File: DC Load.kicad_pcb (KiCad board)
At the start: 2 copper layers, 111 parts, among them IC1 REF7050QDGKR, IC10 REF7050QDGKR, IC11 ISO7740FQDBQRQ1, IC12 ISO7741FQDBQRQ1, IC13 INA826AID, IC14 OPA210IDGKR, IC15 INA296A3IDDFR, IC2 MAX5719GSD+, IC3 REF7050QDGKR, IC4 AD7175-2BRUZ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

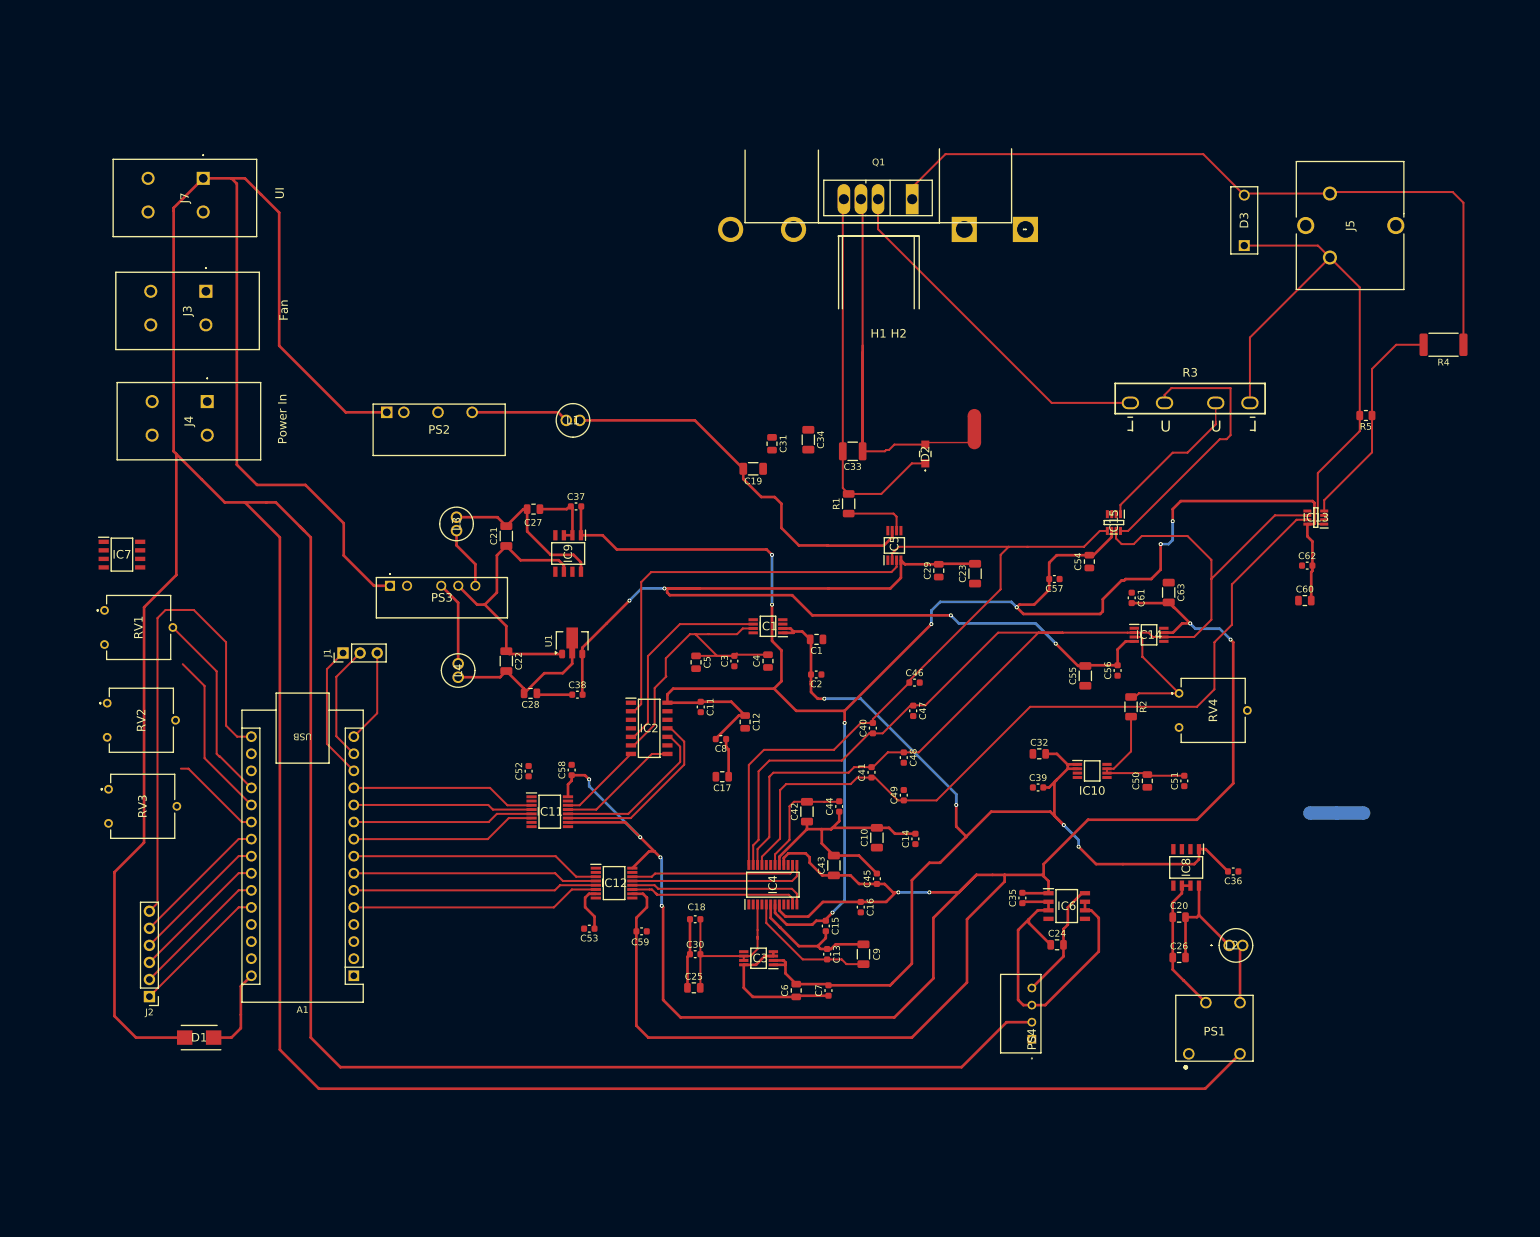
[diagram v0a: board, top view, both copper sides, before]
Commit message: Finished laying out all the traces and adding the temperature sensing circuitry
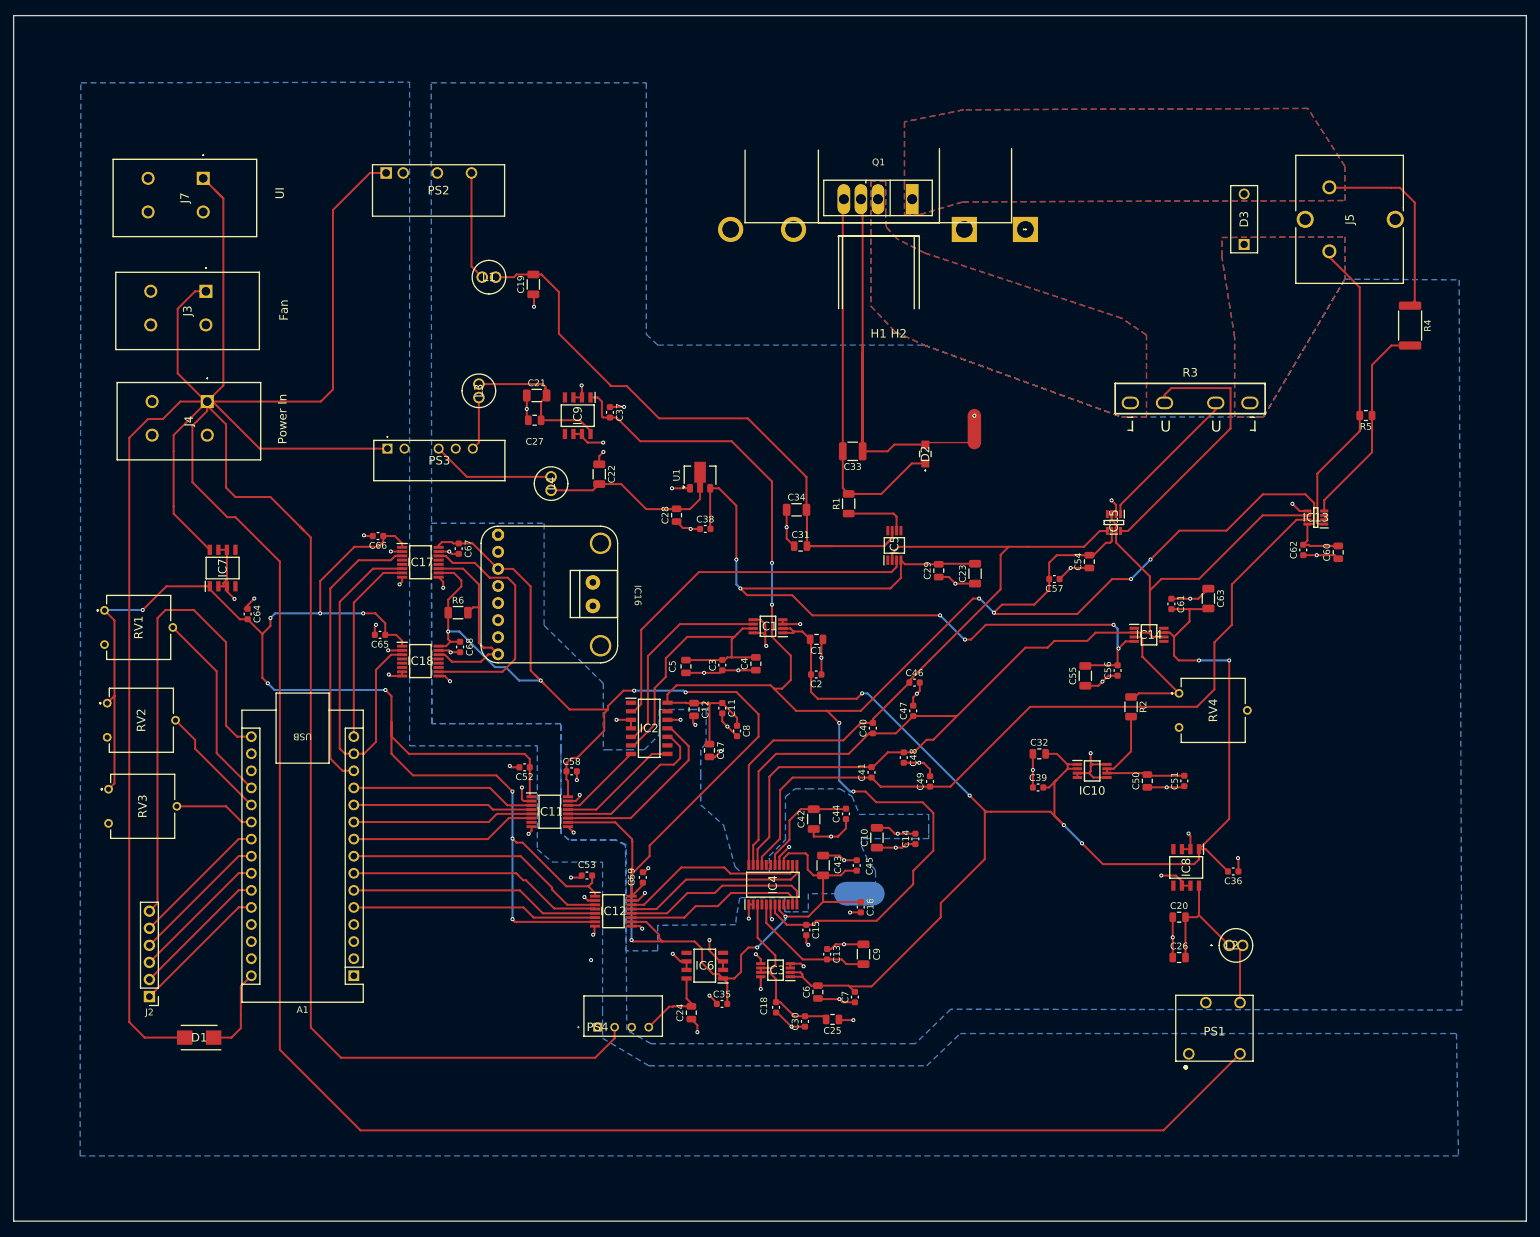
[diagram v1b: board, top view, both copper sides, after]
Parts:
- removed J1: Conn_01x03, Connector_PinHeader_2.54mm:PinHeader_1x03_P2.54mm_Vertical
- removed NT1: Isolated Ground Tie, NetTie:NetTie-3_SMD_Pad2.0mm
- added C64: 0.1u, Capacitor_SMD:C_0603_1608Metric, F.Cu at (69.8, 114.0)
- added C65: 0.1u, Capacitor_SMD:C_0603_1608Metric, F.Cu at (89.5, 117.1)
- added C66: 0.1u, Capacitor_SMD:C_0603_1608Metric, F.Cu at (89.2, 102.4)
- added C67: 0.1u, Capacitor_SMD:C_0603_1608Metric, F.Cu at (101.2, 104.3)
- added C68: 0.1u, Capacitor_SMD:C_0603_1608Metric, F.Cu at (101.4, 118.9)
- added IC16: MAX31850K, Adafruit:MAX31850K, F.Cu at (117.1, 111.2)
- added IC17: ISO7741FQDBQRQ1, ISO7741FQDBQRQ1:SOP64P600X175-16N, F.Cu at (95.5, 106.3)
- added IC18: ISO7741FQDBQRQ1, ISO7741FQDBQRQ1:SOP64P600X175-16N, F.Cu at (95.5, 121.0)
- added NT3: NetTie_2, NetTie:NetTie-2_SMD_Pad2.0mm, B.Cu at (160.8, 155.6)
- added R6: 4.7k, Resistor_SMD:R_1206_3216Metric, F.Cu at (101.1, 113.8)
- moved PS4 64.6 mm to (121.8, 175.4), turned to 0 degrees
- moved C24 55.3 mm to (135.8, 173.3), turned to 90 degrees
- moved IC6 54.6 mm to (137.8, 166.3), turned to 180 degrees
- moved C35 47.4 mm to (140.4, 172.0), turned to 0 degrees
- moved C19 42.7 mm to (112.3, 65.0), turned to 90 degrees
- moved PS2 35.6 mm to (90.4, 48.4)
- moved C28 34.3 mm to (133.6, 99.3), turned to 90 degrees
- moved C38 31.1 mm to (137.9, 101.3)
- moved U1 31.1 mm to (137.1, 93.3)
- moved L4 31.0 mm to (114.9, 95.6)
- moved C22 31.0 mm to (122.1, 93.2)
- moved L1 24.7 mm to (106.7, 63.9)
- moved C21 21.4 mm to (112.8, 81.5), turned to 0 degrees
- moved C25 21.2 mm to (156.8, 174.3), turned to 180 degrees
- moved IC9 20.5 mm to (118.9, 84.5)
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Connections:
- A1 pad 13: Net-(A1-D10/CS) -> Temp Write EN uC
- A1 pad 14: Net-(A1-D11/COPI) -> Temp Sensor uC
- A1 pad 15: Net-(A1-D12/CIPO) -> Temp Read EN uC
- C1 pad 1: AGND Isolated -> GND Isolated
- C10 pad 1: AGND Isolated -> GND Isolated
- C11 pad 2: AGND Isolated -> GND Isolated
- C13 pad 1: AGND Isolated -> GND Isolated
- C14 pad 1: AGND Isolated -> GND Isolated
- C15 pad 2: AGND Isolated -> GND Isolated
- C16 pad 2: AGND Isolated -> GND Isolated
- C17 pad 2: AGND Isolated -> GND Isolated
- C18 pad 2: AGND Isolated -> GND Isolated
- C2 pad 1: AGND Isolated -> GND Isolated
- C23 pad 1: AGND Isolated -> GND Isolated
- C25 pad 1: AGND Isolated -> GND Isolated
- C29 pad 1: AGND Isolated -> GND Isolated
- C3 pad 1: AGND Isolated -> GND Isolated
- C30 pad 1: AGND Isolated -> GND Isolated
- C31 pad 1: AGND Isolated -> GND Isolated
- C32 pad 1: AGND Isolated -> GND Isolated
- C34 pad 1: AGND Isolated -> GND Isolated
- C39 pad 1: AGND Isolated -> GND Isolated
- C4 pad 1: AGND Isolated -> GND Isolated
- C46 pad 2: AGND Isolated -> GND Isolated
- C47 pad 2: AGND Isolated -> GND Isolated
- C48 pad 2: AGND Isolated -> GND Isolated
- C49 pad 2: AGND Isolated -> GND Isolated
- C5 pad 2: AGND Isolated -> GND Isolated
- C50 pad 1: AGND Isolated -> GND Isolated
- C51 pad 1: AGND Isolated -> GND Isolated
- C54 pad 1: AGND Isolated -> GND Isolated
- C55 pad 1: AGND Isolated -> GND Isolated
- C56 pad 1: AGND Isolated -> GND Isolated
- C57 pad 1: AGND Isolated -> GND Isolated
- C6 pad 1: AGND Isolated -> GND Isolated
- C60 pad 1: AGND Isolated -> GND Isolated
- C61 pad 1: AGND Isolated -> GND Isolated
- C61 pad 2: +3.3V Isolated -> +6V Isolated
- C62 pad 1: AGND Isolated -> GND Isolated
- C63 pad 1: AGND Isolated -> GND Isolated
- C63 pad 2: +3.3V Isolated -> +6V Isolated
- C7 pad 1: AGND Isolated -> GND Isolated
- C8 pad 2: AGND Isolated -> GND Isolated
- C9 pad 1: AGND Isolated -> GND Isolated
- IC1 pad 3: AGND Isolated -> GND Isolated
- IC1 pad 4: AGND Isolated -> GND Isolated
- IC1 pad 5: AGND Isolated -> GND Isolated
- IC1 pad 8: AGND Isolated -> GND Isolated
- IC10 pad 3: AGND Isolated -> GND Isolated
- IC10 pad 4: AGND Isolated -> GND Isolated
- IC10 pad 5: AGND Isolated -> GND Isolated
- IC10 pad 8: AGND Isolated -> GND Isolated
- IC13 pad 5: AGND Isolated -> GND Isolated
- IC14 pad 7: +3.3V Isolated -> +6V Isolated
- IC15 pad 2: AGND Isolated -> GND Isolated
- IC2 pad 3: AGND Isolated -> GND Isolated
- IC2 pad 4: AGND Isolated -> GND Isolated
- IC3 pad 3: AGND Isolated -> GND Isolated
- IC3 pad 4: AGND Isolated -> GND Isolated
- IC3 pad 5: AGND Isolated -> GND Isolated
- IC3 pad 8: AGND Isolated -> GND Isolated
- IC4 pad 1: AGND Isolated -> GND Isolated
- IC4 pad 2: AGND Isolated -> GND Isolated
- IC4 pad 6: AGND Isolated -> GND Isolated
- NT2 pad 1: AGND Isolated -> GND Isolated
- RV4 pad 2: AGND Isolated -> GND Isolated
- RV4 pad 3: AGND Isolated -> GND Isolated
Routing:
- net +3.3V: track 7.02 -> 239.9 mm, vias 0 -> 9
- net +3.3V Isolated: track 364.5 -> 260.0 mm
- net in+: track 111.3 -> 30.7 mm
- net GND Isolated: track 130.6 -> 201.0 mm, vias 0 -> 50
- net Temp Sensor uC: track 0.00 -> 55.1 mm
- net Net-(Q1-S): track 52.7 -> 0.00 mm
- net AGND Isolated: track 52.4 -> 0.00 mm
- net +6V Isolated: track 166.2 -> 214.1 mm, vias 4 -> 6
- net Temp Write EN uC: track 0.00 -> 42.3 mm
- net Voltage Sense -: track 88.2 -> 49.3 mm
- net Temp Write EN: track 0.00 -> 36.4 mm
- net GND: track 0.00 -> 34.6 mm, vias 0 -> 15
- net +21V Isolated: track 58.7 -> 92.5 mm
- net Temp Sensor: track 0.00 -> 30.9 mm
- net Temp Read EN uC: track 0.00 -> 29.0 mm
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- added copper zone on B.Cu, net DGND Isolated
- added copper zone on B.Cu, net GND
- added copper zone on B.Cu, net GND Isolated
- added copper zone on B.Cu, net Net-(Q1-S)
- added copper zone on F.Cu, net Net-(Q1-S)
- added copper zone on B.Cu, net Voltage Sense -
- added copper zone on F.Cu, net Voltage Sense -
- added copper zone on B.Cu, net in+
- added copper zone on F.Cu, net in+
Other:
- board outline added: 225 x 179.3 mm

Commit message: Added pdf printouts of the PCB and schematic
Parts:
- moved NT3 4.31 mm to (156.5, 155.9), turned to 90 degrees
- moved NT2 3.91 mm to (174.0, 86.3)
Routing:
- net GND Isolated: track 201.0 -> 41.9 mm, vias 50 -> 61
- net Gate Drive -: track 87.6 -> 52.7 mm
- net DGND Isolated: track 46.5 -> 24.4 mm, vias 16 -> 26
- net GND: track 34.6 -> 18.1 mm, vias 15 -> 30
- net +21V Isolated: track 92.5 -> 88.7 mm
- net +3.3V: track 239.9 -> 237.7 mm
- net +12V: track 689.4 -> 688.5 mm
- net Temp Write EN: track 36.4 -> 37.0 mm
- net +6V Isolated: track 214.1 -> 213.5 mm
- added copper zone on F.Cu, net DGND Isolated
- added copper zone on F.Cu, net GND
- added copper zone on F.Cu, net GND Isolated

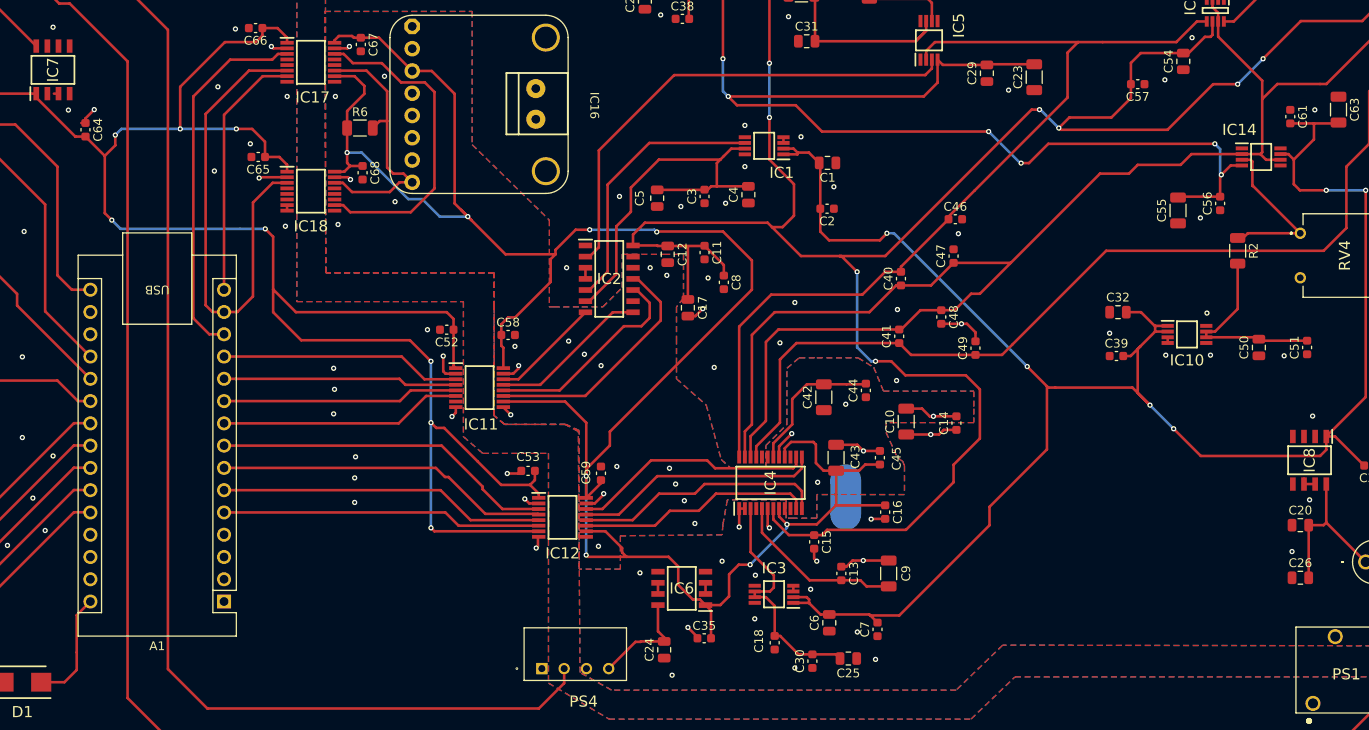
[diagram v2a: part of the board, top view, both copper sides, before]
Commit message: improved the connection to the temp sensor
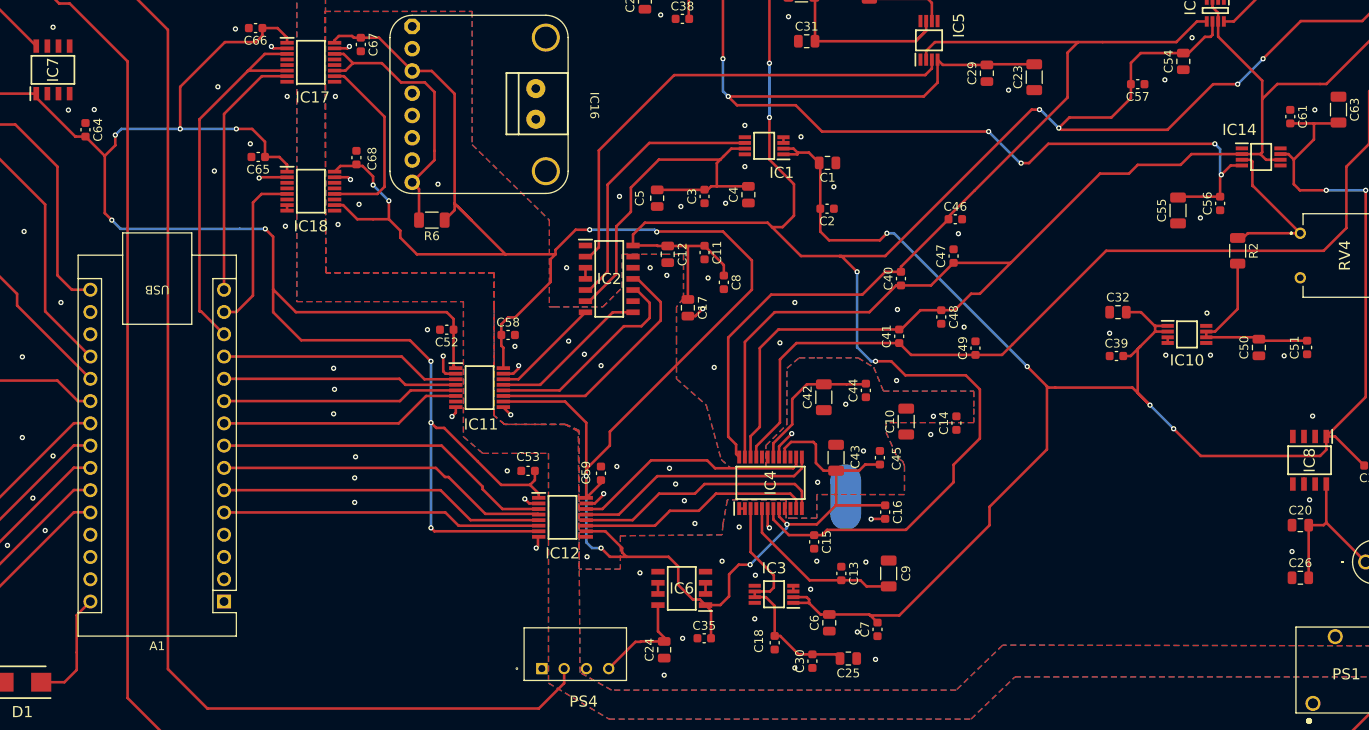
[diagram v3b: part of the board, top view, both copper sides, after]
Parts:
- moved R6 13.3 mm to (109.3, 124.3), turned to 180 degrees
- moved C68 1.86 mm to (100.7, 117.2), turned to 90 degrees
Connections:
- A1 pad 13: Temp Write EN uC -> Temp Sensor uC
- A1 pad 14: Temp Sensor uC -> Temp Write EN uC
- IC17 pad 10: +3.3V Isolated -> Temp Write EN
- IC17 pad 14: Temp Write EN -> Temp Sensor
- IC17 pad 3: Temp Write EN uC -> Temp Sensor uC
- IC18 pad 10: Temp Write EN -> +3.3V Isolated
- IC18 pad 12: unconnected-(IC18-OUTC-Pad12) -> Temp Write EN
- IC18 pad 14: Temp Sensor -> unconnected-(IC18-OUTA-Pad14)
- IC18 pad 3: Temp Sensor uC -> unconnected-(IC18-INA-Pad3)
- IC18 pad 5: unconnected-(IC18-INC-Pad5) -> Temp Write EN uC
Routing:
- net GND Isolated: track 41.9 -> 18.4 mm
- net Temp Write EN uC: track 42.3 -> 19.0 mm
- net Temp Write EN: track 37.0 -> 21.6 mm
- net Temp Sensor uC: track 55.1 -> 43.5 mm
- net DGND Isolated: track 24.4 -> 13.0 mm
- net GND: track 18.1 -> 13.9 mm, vias 30 -> 31
- net Current Sense Amp Out: track 104.9 -> 105.9 mm
- net +3.3V Isolated: track 259.6 -> 260.6 mm
- net Temp Sensor: track 30.9 -> 31.6 mm
